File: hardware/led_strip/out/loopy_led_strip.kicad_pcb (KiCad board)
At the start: 2 copper layers, 75 x 8 mm, 8 parts, among them J1 castellated_edge, J2 castellated_edge

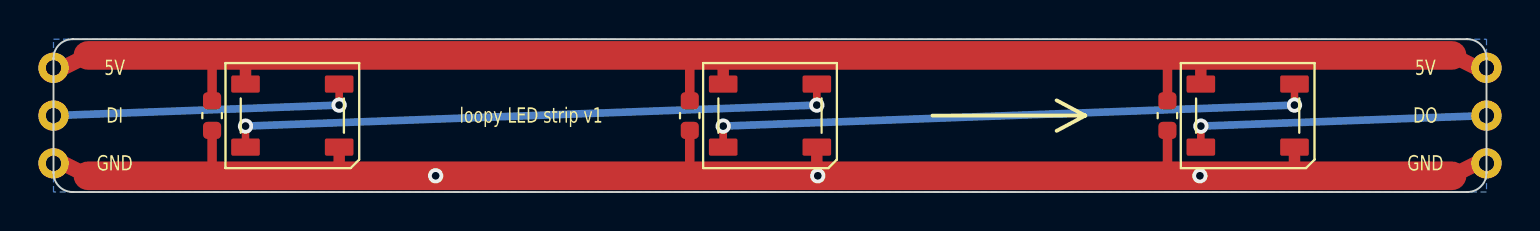
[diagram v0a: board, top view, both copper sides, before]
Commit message: feat(hardware): shrink indicators to single-LED pucks + pill diffusers
Per review: pedal-width strips were too wide. Each indicator is now ONE
WS2812B 5050 behind a small 15x6 pill diffuser slot (same per-pedal
centre-line), and the board shrinks to a 16x8mm single-LED puck --
N_LEDS/LED_PITCH stay parametric; the shrink exposed and fixed three
more scale-dependent leftovers (hop-clearance assert applies only when
LEDs chain on-board, GND stitching vias now derive from the LED gaps,
end labels hug the pads on short boards). DRC clean (0 violations, 0
unconnected); render verified; gerbers + JLC zip regenerated.

Fusion: faceplate rebuilt with the pill slots; populated console shows
one glowing pill + puck PCB + single 5050 per indicator pedal.

Refs #239
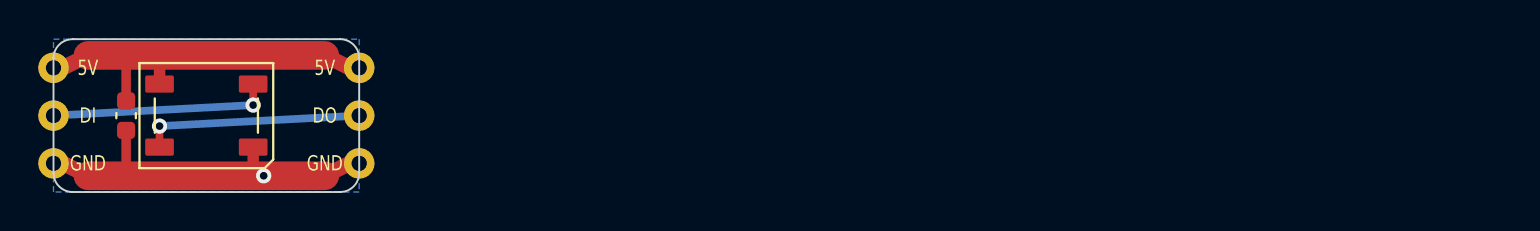
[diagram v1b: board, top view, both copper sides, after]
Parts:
- removed C2, C3: C_0603_1608Metric, C_0603_1608Metric
- removed D2, D3: LED_WS2812B_PLCC4_5.0x5.0mm_P3.2mm, LED_WS2812B_PLCC4_5.0x5.0mm_P3.2mm
- moved J2 59.0 mm to (66.0, 54.0)
- moved C1 4.50 mm to (53.8, 54.0)
- moved D1 4.50 mm to (58.0, 54.0)
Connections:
- D1 pad 2: D12 -> DOUT
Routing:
- net GND: track 85.9 -> 19.2 mm, vias 3 -> 1
- net +5V: track 85.9 -> 19.2 mm
- net D23: track 32.1 -> 0.00 mm, vias 2 -> 0
- net D12: track 32.1 -> 0.00 mm, vias 2 -> 0
- net DOUT: track 16.1 -> 11.6 mm
- net DIN: track 16.1 -> 11.6 mm
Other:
- board size 75 x 8 mm -> 16 x 8 mm
- board text removed: "loopy LED strip v1"
